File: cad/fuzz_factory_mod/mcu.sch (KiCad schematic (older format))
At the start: 20 parts, among them J201 Conn_MCU_SWD, U201 STM32F303VCTx, Y201 Resonator_Small

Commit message: Commit pre- board separation.
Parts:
- added J202: Conn_interface_1, Pin_Headers:Pin_Header_Straight_1x12_Pitch2.54mm_SMD_Pin1Left, symbol Connector:Conn_01x12_Female
- added J203: Conn_interface_2, Pin_Headers:Pin_Header_Straight_1x12_Pitch2.54mm_SMD_Pin1Left, symbol Connector:Conn_01x12_Female
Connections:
- net labels added: +5V, ENC3_BTN, ENC3_IN_CCW, ENC3_IN_CW, ENC3_LED_GREEN, ENC3_LED_RED
- wire segments 168 -> 178
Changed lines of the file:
@@
 F21 "ENC3_ENC2" I L 10000 3550 50
 $EndSheet
-Text Label 9900 1600 2    50   ~ 0
+Text Label 8400 1600 2    50   ~ 0
 SPI2_SCK
-Text Label 9900 1700 2    50   ~ 0
+Text Label 8400 1700 2    50   ~ 0
 SPI2_MOSI
 Wire Wire Line
-	10000 1600 9500 1600
-Wire Wire Line
-	10000 1700 9500 1700
-Text Label 9900 2700 2    50   ~ 0
+	8500 1600 8000 1600
+Wire Wire Line
+	8500 1700 8000 1700
+Text Label 8400 3100 2    50   ~ 0
 ENC2_LED_RED
-Text Label 9900 2800 2    50   ~ 0
+Text Label 8400 3200 2    50   ~ 0
 ENC2_LED_GREEN
-Text Label 9900 2600 2    50   ~ 0
+Text Label 8400 3000 2    50   ~ 0
 ENC2_BTN
-Text Label 9900 2900 2    50   ~ 0
+Text Label 8400 3300 2    50   ~ 0
 ENC2_IN_CW
-Text Label 9900 2050 2    50   ~ 0
+Text Label 8400 2100 2    50   ~ 0
 ENC1_BTN
-Text Label 9900 2350 2    50   ~ 0
+Text Label 8400 2400 2    50   ~ 0
 ENC1_IN_CW
-Text Label 9900 2450 2    50   ~ 0
+Text Label 8400 2500 2    50   ~ 0
 ENC1_IN_CCW
-Text Label 9900 2150 2    50   ~ 0
+Text Label 8400 2200 2    50   ~ 0
 ENC1_LED_RED
-Text Label 9900 2250 2    50   ~ 0
+Text Label 8400 2300 2    50   ~ 0
 ENC1_LED_GREEN
-Text Label 9900 3000 2    50   ~ 0
+Text Label 8400 3400 2    50   ~ 0
 ENC2_IN_CCW
 Wire Wire Line
-	10000 2050 9500 2050
-Wire Wire Line
-	10000 2150 9500 2150
-Wire Wire Line
-	10000 2250 9500 2250
-Wire Wire Line
-	10000 2350 9500 2350
-Wire Wire Line
-	10000 2450 9500 2450
-Wire Wire Line
-	10000 2600 9500 2600
-Wire Wire Line
-	10000 2700 9500 2700
-Wire Wire Line
-	10000 2800 9500 2800
-Wire Wire Line
-	10000 2900 9500 2900
-Wire Wire Line
-	10000 3000 9500 3000
+	8500 2100 8000 2100
+Wire Wire Line
+	8500 2200 8000 2200
+Wire Wire Line
+	8500 2300 8000 2300
+Wire Wire Line
+	8500 2400 8000 2400
+Wire Wire Line
+	8500 2500 8000 2500
+Wire Wire Line
+	8500 3000 8000 3000
+Wire Wire Line
+	8500 3100 8000 3100
+Wire Wire Line
+	8500 3200 8000 3200
+Wire Wire Line
+	8500 3300 8000 3300
+Wire Wire Line
+	8500 3400 8000 3400
 $Sheet
 S 10000 4250 1000 500
@@
 Text Label 5450 4150 0    50   ~ 0
 DISP_LATCH
-Text Label 9900 1900 2    50   ~ 0
+Text Label 8400 1900 2    50   ~ 0
 DISP_LATCH
-Text Label 9900 1800 2    50   ~ 0
+Text Label 8400 1800 2    50   ~ 0
 DISP_ENABLE
 Wire Wire Line
-	10000 1800 9500 1800
-Wire Wire Line
-	10000 1900 9500 1900
+	8500 1800 8000 1800
+Wire Wire Line
+	8500 1900 8000 1900
 Wire Wire Line
 	5350 4150 6500 4150
@@
 Text GLabel 6500 4350 2    50   Input ~ 0
 INPUT_CAPTURE_3
+$Comp
+L Connector:Conn_01x12_Female J202
+U 1 1 5ED776C7
+P 8700 2000
+F 0 "J202" H 8728 1976 50  0000 L CNN
+F 1 "Conn_interface_1" H 8300 1300 50  0000 L CNN
+F 2 "Pin_Headers:Pin_Header_Straight_1x12_Pitch2.54mm_SMD_Pin1Left" H 8700 2000 50  0001 C CNN
+F 3 "~" H 8700 2000 50  0001 C CNN
+	1    8700 2000
+	1    0    0    -1
+$EndComp
+$Comp
+L Connector:Conn_01x12_Female J203
+U 1 1 5ED79A9E
+P 8700 3400
+F 0 "J203" H 8728 3376 50  0000 L CNN
+F 1 "Conn_interface_2" H 8300 2700 50  0000 L CNN
+F 2 "Pin_Headers:Pin_Header_Straight_1x12_Pitch2.54mm_SMD_Pin1Left" H 8700 3400 50  0001 C CNN
+F 3 "~" H 8700 3400 50  0001 C CNN
+	1    8700 3400
+	1    0    0    -1
+$EndComp
+Text Label 8400 3700 2    50   ~ 0
+ENC3_LED_RED
+Text Label 8400 3800 2    50   ~ 0
+ENC3_LED_GREEN
+Text Label 8400 3600 2    50   ~ 0
+ENC3_BTN
+Text Label 8400 3900 2    50   ~ 0
+ENC3_IN_CW
+Text Label 8400 4000 2    50   ~ 0
+ENC3_IN_CCW
+Wire Wire Line
+	8500 3600 8000 3600
+Wire Wire Line
+	8500 3700 8000 3700
+Wire Wire Line
+	8500 3800 8000 3800
+Wire Wire Line
+	8500 3900 8000 3900
+Wire Wire Line
+	8500 4000 8000 4000
+$Comp
+L power:GNDD #PWR0227
+U 1 1 5EDA6D92
+P 8000 1500
+F 0 "#PWR0227" H 8000 1250 50  0001 C CNN
+F 1 "GNDD" V 8004 1390 50  0000 R CNN
+F 2 "" H 8000 1500 50  0001 C CNN
+F 3 "" H 8000 1500 50  0001 C CNN
+	1    8000 1500
+	0    1    1    0
+$EndComp
+Wire Wire Line
+	8500 1500 8000 1500
+$Comp
+L power:GNDD #PWR0236
+U 1 1 5EDB1D7C
+P 8000 2900
+F 0 "#PWR0236" H 8000 2650 50  0001 C CNN
+F 1 "GNDD" V 8004 2790 50  0000 R CNN
+F 2 "" H 8000 2900 50  0001 C CNN
+F 3 "" H 8000 2900 50  0001 C CNN
+	1    8000 2900
+	0    1    1    0
+$EndComp
+Wire Wire Line
+	8500 2900 8000 2900
+$Comp
+L power:+3.3V #PWR0259
+U 1 1 5EDC43BD
+P 8000 2600
+F 0 "#PWR0259" H 8000 2450 50  0001 C CNN
+F 1 "+3.3V" V 8015 2728 50  0000 L CNN
+F 2 "" H 8000 2600 50  0001 C CNN
+F 3 "" H 8000 2600 50  0001 C CNN
+	1    8000 2600
+	0    -1   -1   0
+$EndComp
+Wire Wire Line
+	8000 2000 8500 2000
+$Comp
+L power:+5V #PWR0260
+U 1 1 5EDD067C
+P 8000 2000
+F 0 "#PWR0260" H 8000 1850 50  0001 C CNN
+F 1 "+5V" V 8015 2128 50  0000 L CNN
+F 2 "" H 8000 2000 50  0001 C CNN
+F 3 "" H 8000 2000 50  0001 C CNN
+	1    8000 2000
+	0    -1   -1   0
+$EndComp
+Wire Wire Line
+	8500 2600 8000 2600
+$Comp
+L power:+3.3V #PWR0261
+U 1 1 5EDDC1B4
+P 8000 3500
+F 0 "#PWR0261" H 8000 3350 50  0001 C CNN
+F 1 "+3.3V" V 8015 3628 50  0000 L CNN
+F 2 "" H 8000 3500 50  0001 C CNN
+F 3 "" H 8000 3500 50  0001 C CNN
+	1    8000 3500
+	0    -1   -1   0
+$EndComp
+Wire Wire Line
+	8500 3500 8000 3500
 $EndSCHEMATC

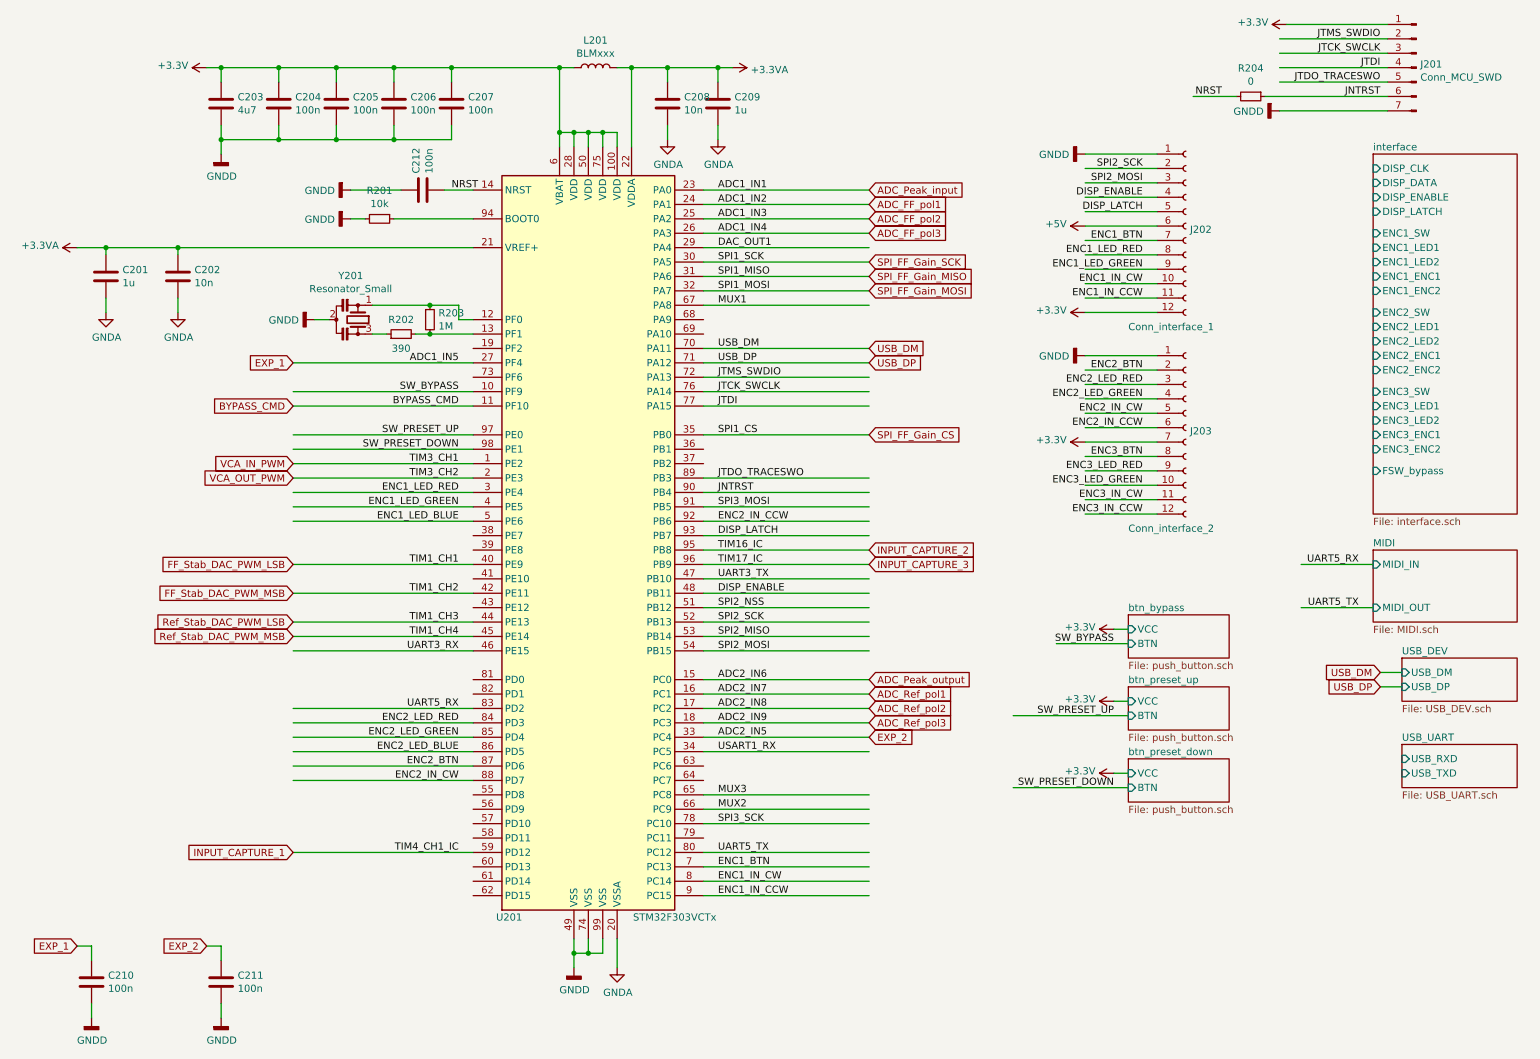
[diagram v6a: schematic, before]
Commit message: Changes architecture.
Corrections on schematic.
Continued Layout placement.
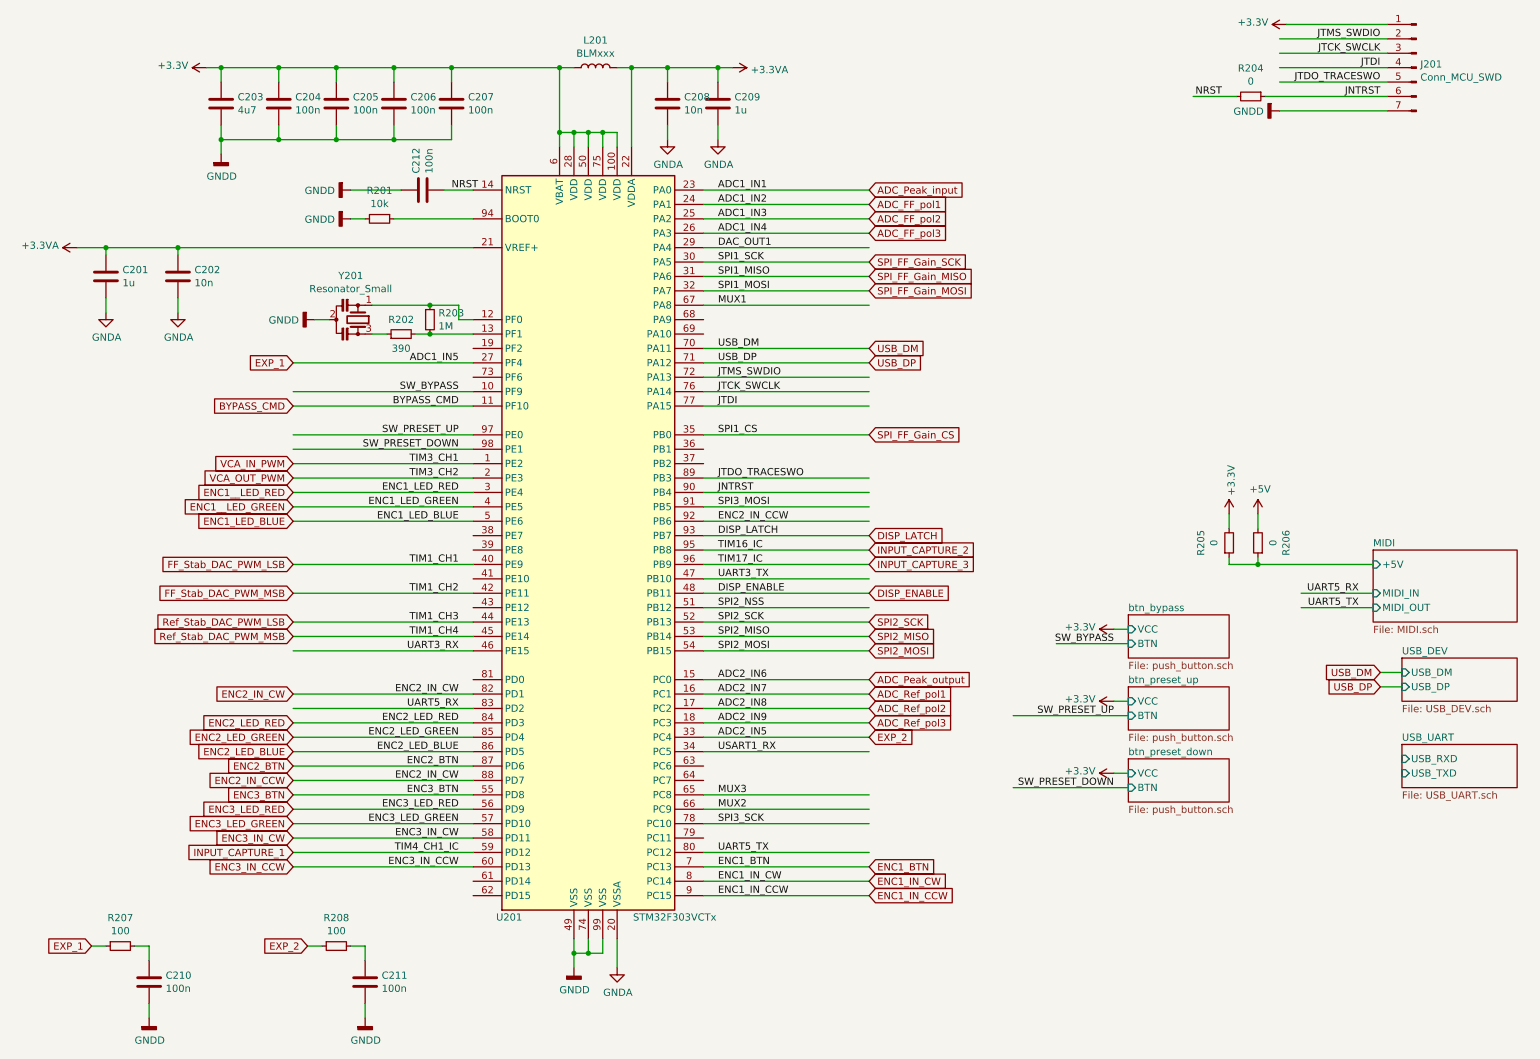
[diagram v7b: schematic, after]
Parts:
- removed J202: Conn_interface_1, Pin_Headers:Pin_Header_Straight_1x12_Pitch2.54mm_SMD_Pin1Left, symbol Connector:Conn_01x12_Female
- removed J203: Conn_interface_2, Pin_Headers:Pin_Header_Straight_1x12_Pitch2.54mm_SMD_Pin1Left, symbol Connector:Conn_01x12_Female
- added R205, R206: 0, Resistors_SMD:R_0603, symbol Device:R_Small
- added R207, R208: 100, Resistors_SMD:R_0603, symbol Device:R_Small
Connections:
- net labels added: ENC1__LED_GREEN, ENC1__LED_RED
- wire segments 178 -> 168
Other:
- moved on the sheet: C210, C211

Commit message: Continued layout.
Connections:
- net labels added: USART1_TX
- wire segments 168 -> 171
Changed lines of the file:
@@
 EESchema Schematic File Version 4
-LIBS:fuzz_factory_mod-cache
 EELAYER 30 0
 EELAYER END
@@
 Wire Wire Line
 	2600 7000 2700 7000
+Text Label 10100 5700 2    50   ~ 0
+USART1_RX
+Text Label 5450 2650 0    50   ~ 0
+USART1_TX
+Wire Wire Line
+	5350 2650 6500 2650
+Text Label 10100 5800 2    50   ~ 0
+USART1_TX
+Wire Wire Line
+	10200 5800 9650 5800
+Wire Wire Line
+	10200 5700 9650 5700
 $EndSCHEMATC
